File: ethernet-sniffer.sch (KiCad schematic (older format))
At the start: 3 parts, among them J101 Conn_01x06, J102 USB_B_Micro, J103 POWER 5V

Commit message: Cleanup
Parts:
- removed J101: Conn_01x06, Connector_PinHeader_2.54mm:PinHeader_1x06_P2.54mm_Vertical, symbol Connector_Generic:Conn_01x06
- added J101: Conn_01x08, Connector_PinHeader_2.54mm:PinHeader_1x08_P2.54mm_Vertical, symbol Connector_Generic:Conn_01x08
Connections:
- wire segments 114 -> 118
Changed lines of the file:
@@
 F23 "SPI1_MISO" I R 3000 4850 50
 F24 "SPI1_MOSI" O R 3000 4950 50
+F25 "STM_3V3" U L 1950 4000 50
 $EndSheet
 NoConn ~ 4050 1700
@@
 NoConn ~ 7950 5500
 Wire Wire Line
-	1950 3200 1400 3200
-Wire Wire Line
-	1950 3300 1400 3300
+	1950 3200 1200 3200
+Wire Wire Line
+	1950 3300 1200 3300
 Wire Wire Line
 	1950 3500 1800 3500
@@
 	1800 3500 1800 3400
 Wire Wire Line
-	1800 3400 1400 3400
+	1800 3400 1200 3400
 Wire Wire Line
 	1950 3600 1700 3600
@@
 	1700 3600 1700 3500
 Wire Wire Line
-	1700 3500 1400 3500
+	1700 3500 1200 3500
 Wire Wire Line
 	1950 3800 1600 3800
@@
 	1600 3800 1600 3600
 Wire Wire Line
-	1600 3600 1400 3600
-Wire Wire Line
-	1400 3700 1500 3700
+	1600 3600 1200 3600
+Wire Wire Line
+	1200 3700 1500 3700
 Wire Wire Line
 	1500 3700 1500 3900
@@
 Wire Wire Line
 	5750 4950 3000 4950
-$Comp
-L Connector_Generic:Conn_01x06 J101
-U 1 1 5FE97580
-P 1200 3400
-F 0 "J101" H 1118 3817 50  0000 C CNN
-F 1 "Conn_01x06" H 1118 3726 50  0000 C CNN
-F 2 "Connector_PinHeader_2.54mm:PinHeader_1x06_P2.54mm_Vertical" H 1200 3400 50  0001 C CNN
-F 3 "~" H 1200 3400 50  0001 C CNN
-	1    1200 3400
-	-1   0    0    -1
-$EndComp
 $Sheet
 S 4650 2600 700  1500
@@
 $EndComp
 Wire Wire Line
-	4250 1150 4250 1050
+	4250 1150 4250 1100
 $Comp
 L power:GNDD #PWR0117
@@
 Wire Wire Line
 	4350 1150 4350 1050
+$Comp
+L Connector_Generic:Conn_01x08 J101
+U 1 1 5EEB686D
+P 1000 3600
+F 0 "J101" H 918 2975 50  0000 C CNN
+F 1 "Conn_01x08" H 918 3066 50  0000 C CNN
+F 2 "Connector_PinHeader_2.54mm:PinHeader_1x08_P2.54mm_Vertical" H 1000 3600 50  0001 C CNN
+F 3 "~" H 1000 3600 50  0001 C CNN
+	1    1000 3600
+	-1   0    0    1
+$EndComp
+$Comp
+L power:GNDD #PWR0118
+U 1 1 5EEBC6EA
+P 1200 3900
+F 0 "#PWR0118" H 1200 3650 50  0001 C CNN
+F 1 "GNDD" H 1204 3745 50  0000 C CNN
+F 2 "" H 1200 3900 50  0001 C CNN
+F 3 "" H 1200 3900 50  0001 C CNN
+	1    1200 3900
+	0    -1   -1   0
+$EndComp
+Wire Wire Line
+	1200 3800 1400 3800
+Wire Wire Line
+	1400 3800 1400 4000
+Wire Wire Line
+	1400 4000 1950 4000
+$Comp
+L power:PWR_FLAG #FLG0104
+U 1 1 5EF1E78A
+P 4250 1100
+F 0 "#FLG0104" H 4250 1175 50  0001 C CNN
+F 1 "PWR_FLAG" V 4250 1227 50  0000 L CNN
+F 2 "" H 4250 1100 50  0001 C CNN
+F 3 "~" H 4250 1100 50  0001 C CNN
+	1    4250 1100
+	0    -1   -1   0
+$EndComp
+Connection ~ 4250 1100
+Wire Wire Line
+	4250 1100 4250 1050
 $EndSCHEMATC

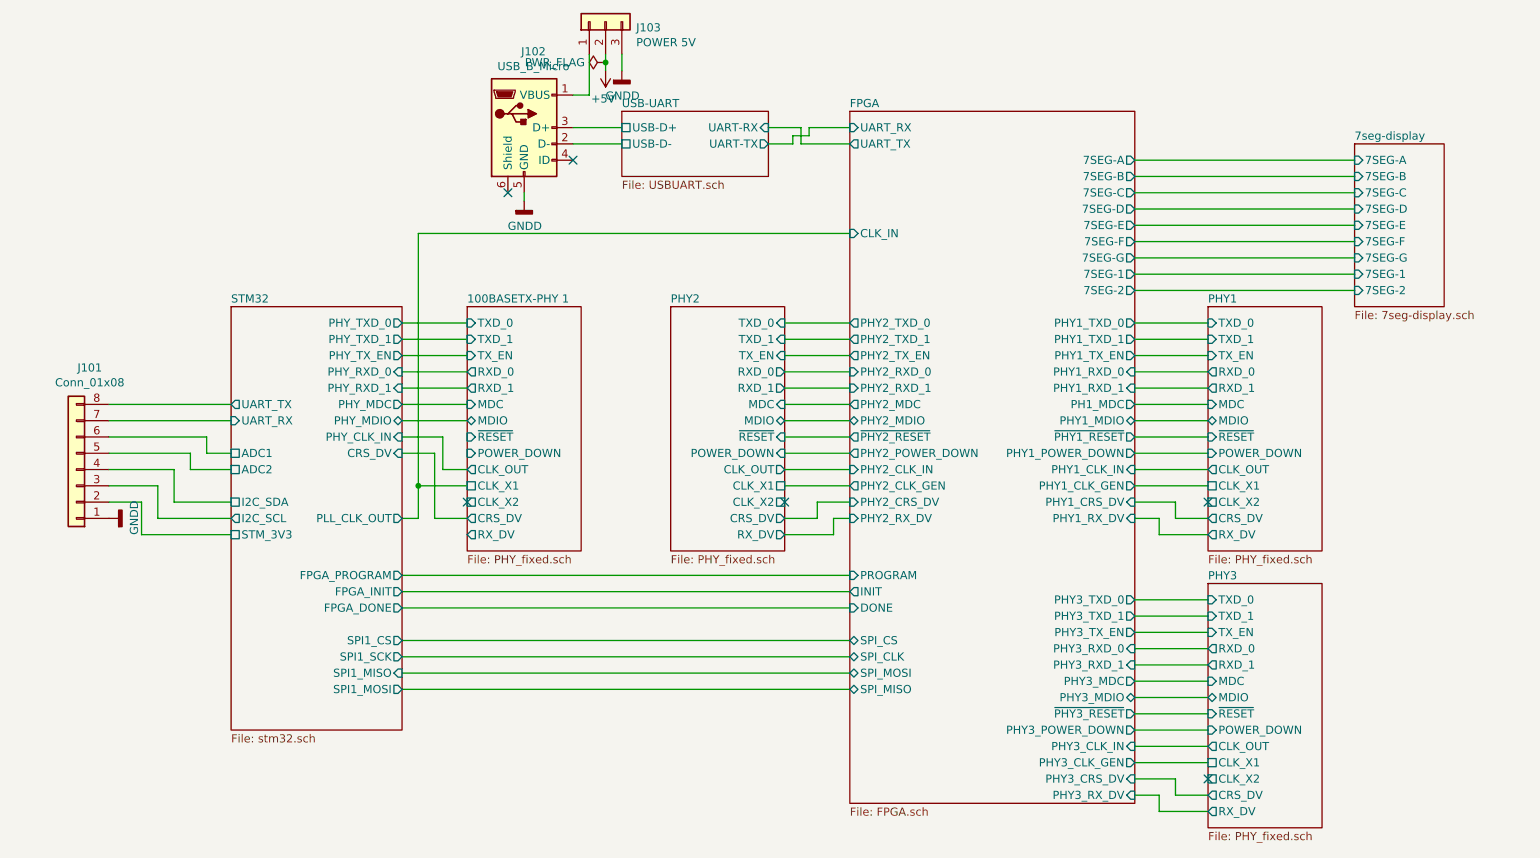
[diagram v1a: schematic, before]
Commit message: PCB layout 90% finished
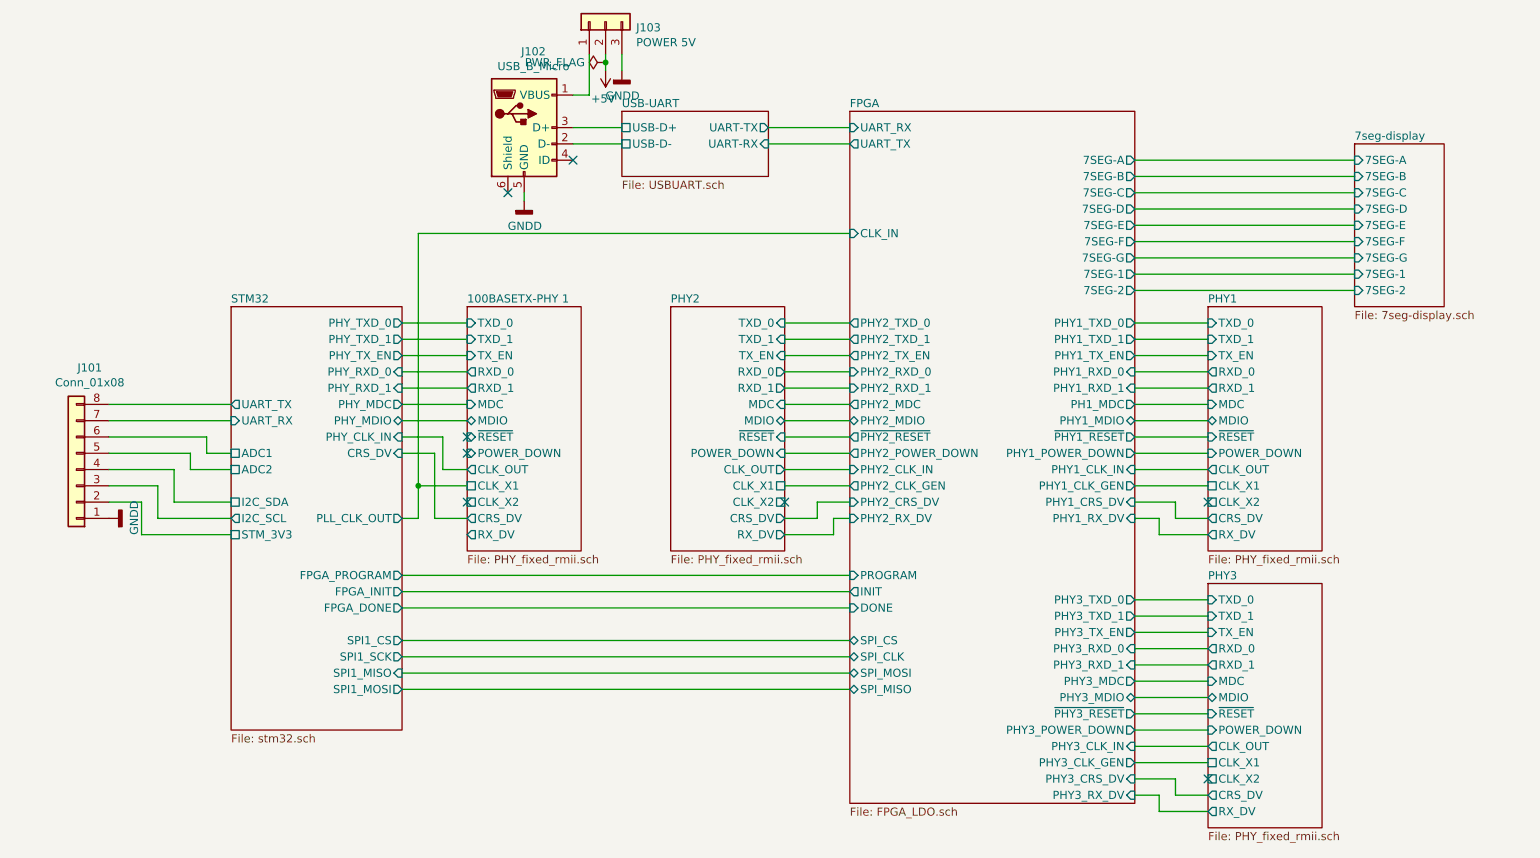
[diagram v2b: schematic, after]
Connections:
- no-connect marks 6 -> 8
